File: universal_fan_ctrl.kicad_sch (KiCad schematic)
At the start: 14 parts, among them J1 Conn_01x03, J2 Conn_01x02, Q1 DMG3406L, U1 TLV76033DBZ, U2 ATtiny202-SS, U3 DS18B20

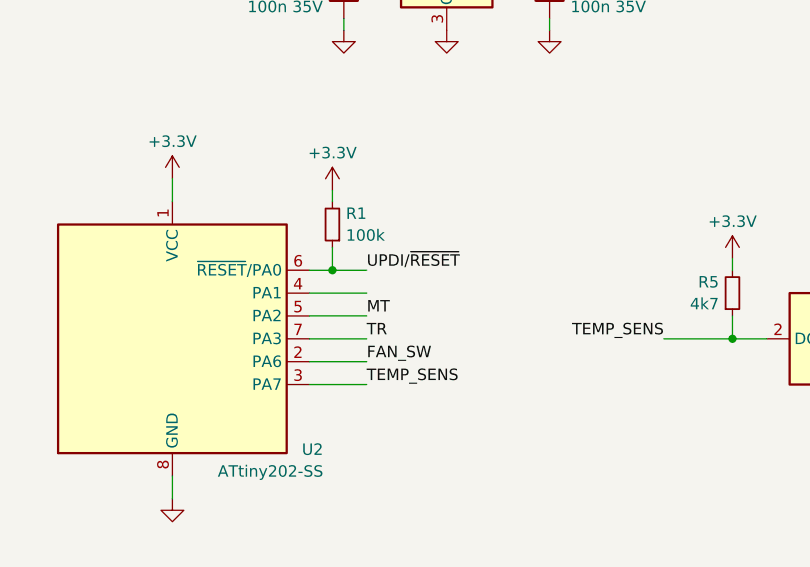
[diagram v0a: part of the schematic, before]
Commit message: Connected FAN_CTRL net to the spare AVR pin
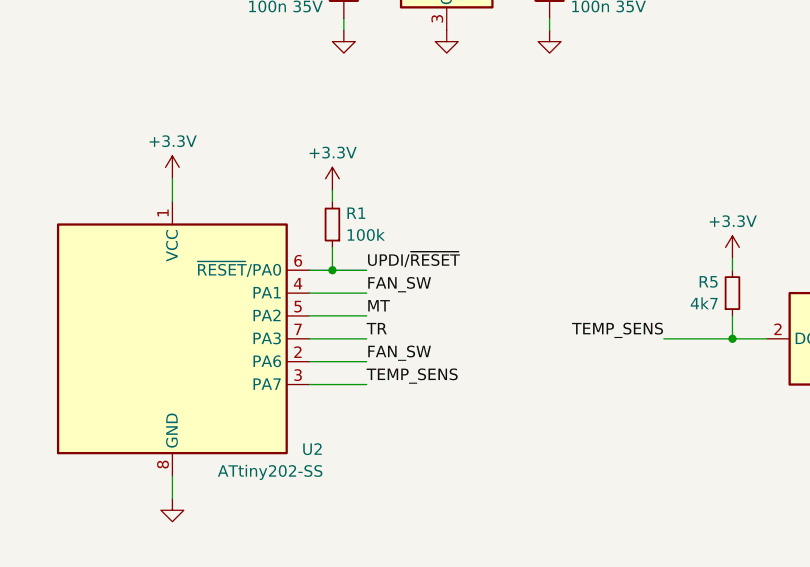
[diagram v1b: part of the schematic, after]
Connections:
- net FAN_SW: now also U2.4 (PA1)
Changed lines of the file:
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@@
+		)
+	)
+	(label "FAN_SW"
+		(at 78.74 87.63 0)
+		(fields_autoplaced yes)
+		(effects
+			(font
+				(size 1.27 1.27)
+			)
+			(justify left bottom)
 		)
 	)

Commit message: kicad update, addressing #1
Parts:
- removed C1: 100n 35V, Resistor_SMD:R_0603_1608Metric, symbol Device:C_Small
- removed R1: 100k, Resistor_SMD:R_0603_1608Metric, symbol Device:R_Small
- added D2: BAT54J, Diode_SMD:D_SOD-323F, symbol Diode:BAT54J
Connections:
- net at J1.1 (Pin_1), J2.1 (Pin_1), U1.2 (VI): now also D2.1 (K)
- net at J2.2 (Pin_2), Q1.3 (D): now also D2.2 (A)
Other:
- note added: "Temperature ramp (Tmax-x) (Rtr): 2.5C - OPEN 5C - 33k 10C - 12k 20C - 2k7 or less"
- note removed: "Temperature ramp (Tmax-x) (Rtr): 5C - OPEN 10C - 33k 15C - 12k 20C - 2k7 or less"
- moved on the sheet: J2, Q1
